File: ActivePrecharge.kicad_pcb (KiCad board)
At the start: 2 copper layers, 71 x 55 mm, 34 parts, among them Con1 LED, J1 Conn_01x03, J2 Conn_01x02, J3 Conn_01x02, Q1 IRLML0030, U1 NCP785AH50T1G, U2 NCP785AH50T1G, U3 TLV9301xDCK, U4 TCMT1106

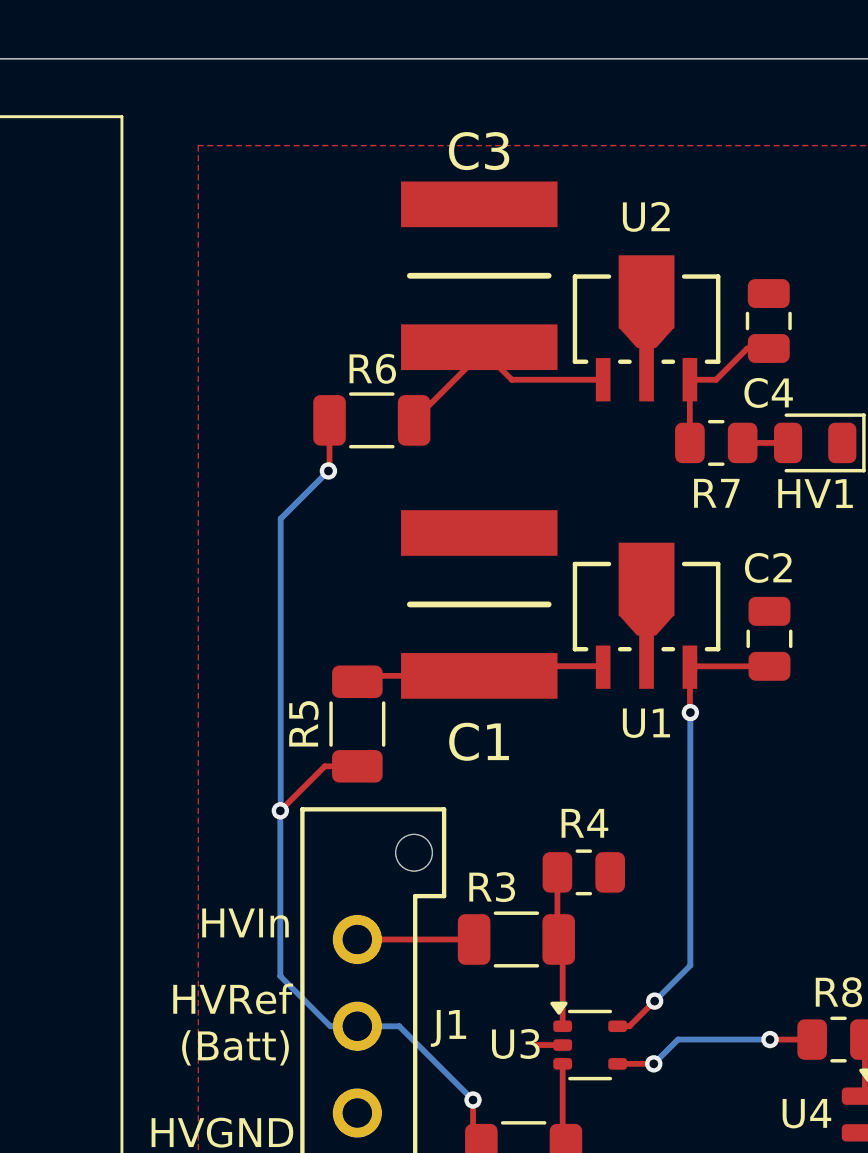
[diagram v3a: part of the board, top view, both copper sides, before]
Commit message: revert LDO HV resistor position
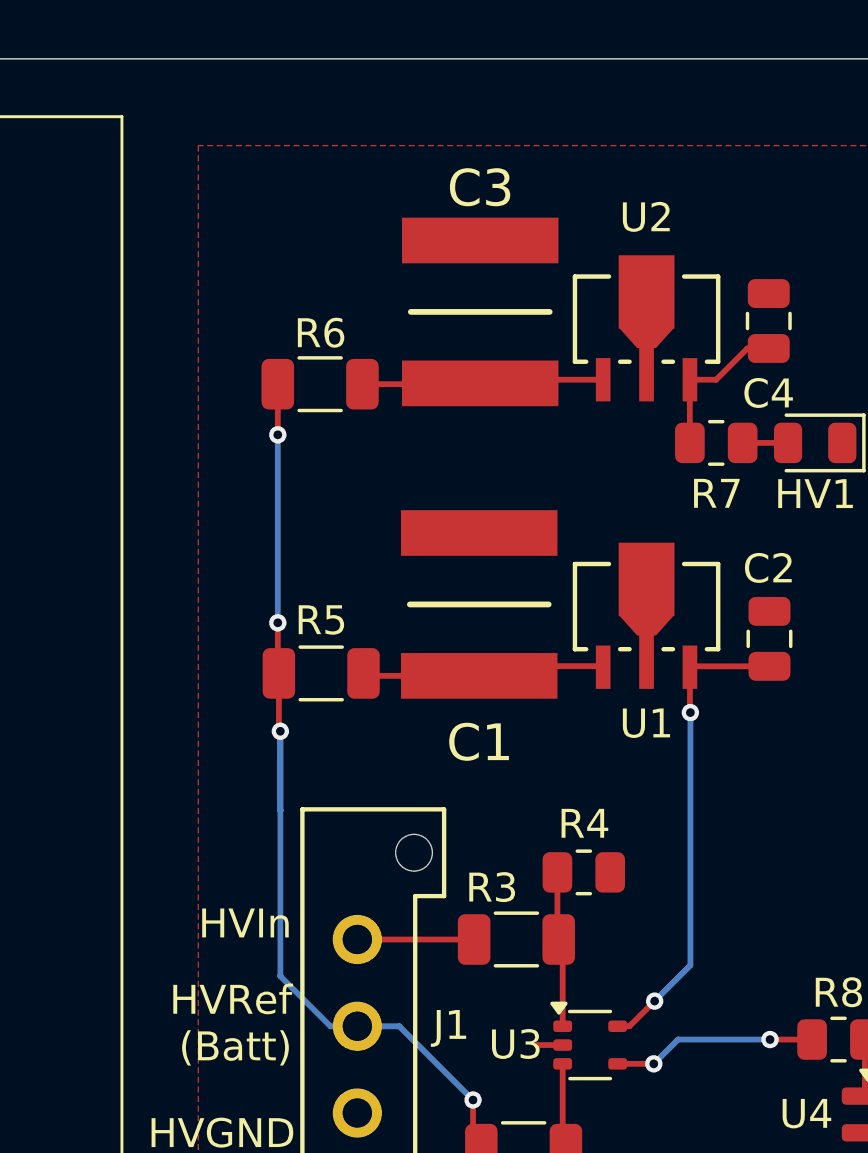
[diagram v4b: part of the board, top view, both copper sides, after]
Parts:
- moved R6 2.18 mm to (105.2, 79.2)
- moved R5 2.15 mm to (105.2, 89.2), turned to 0 degrees
- moved C3 1.25 mm to (110.8, 76.8)
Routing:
- net HVRef: track 33.5 -> 31.8 mm, vias 3 -> 4
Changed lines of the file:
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@@
 	(footprint "Active-PrechargeLib:CAPC5750X220N"
 		(layer "F.Cu")
-		(at 110.7155 75.5 90)
+		(at 110.75 76.75 90)
 		(descr "2220-1")
 		(tags "Capacitor")
@@
 	(footprint "Resistor_SMD:R_1206_3216Metric"
 		(layer "F.Cu")
-		(at 106.5 91 90)
+		(at 105.25 89.25)
 		(descr "Resistor SMD 1206 (3216 Metric), square (rectangular) end terminal, IPC_7351 nominal, (Body size source: IPC-SM-782 page 72, https://www.pcb-3d.com/wordpress/wp-content/uploads/ipc-sm-782a_amendment_1_and_2.pdf), generated with kicad-footprint-generator")
 		(tags "resistor")
 		(property "Reference" "R5"
-			(at 0 -1.82 90)
+			(at 0 -1.82 360)
 			(layer "F.SilkS")
 			(effects
@@
 		)
 		(property "Value" "10k"
-			(at 0 1.82 90)
+			(at 0 1.82 360)
 			(layer "F.Fab")
 			(effects
@@
 		)
 		(property "Footprint" "Resistor_SMD:R_1206_3216Metric"
-			(at 0 0 90)
+			(at 0 0 0)
 			(unlocked yes)
 			(layer "F.Fab")
@@
 		)
 		(property "Datasheet" ""
-			(at 0 0 90)
+			(at 0 0 0)
 			(unlocked yes)
 			(layer "F.Fab")
@@
 		)
 		(property "Description" "Resistor, US symbol"
-			(at 0 0 90)
+			(at 0 0 0)
 			(unlocked yes)
 			(layer "F.Fab")
@@
 		)
 		(fp_line
-			(start 2.28 -1.12)
-			(end 2.28 1.12)
+			(start -2.28 -1.12)
+			(end 2.28 -1.12)
 			(stroke
 				(width 0.05)
@@
 		)
 		(fp_line
-			(start -2.28 -1.12)
-			(end 2.28 -1.12)
+			(start -2.28 1.12)
+			(end -2.28 -1.12)
 			(stroke
 				(width 0.05)
@@
 		)
 		(fp_line
-			(start 2.28 1.12)
-			(end -2.28 1.12)
+			(start 2.28 -1.12)
+			(end 2.28 1.12)
 			(stroke
 				(width 0.05)
@@
 		)
 		(fp_line
-			(start -2.28 1.12)
-			(end -2.28 -1.12)
+			(start 2.28 1.12)
+			(end -2.28 1.12)
 			(stroke
 				(width 0.05)
@@
 		)
 		(fp_line
-			(start 1.6 -0.8)
-			(end 1.6 0.8)
+			(start -1.6 -0.8)
+			(end 1.6 -0.8)
 			(stroke
 				(width 0.1)
@@
 		)
 		(fp_line
-			(start -1.6 -0.8)
-			(end 1.6 -0.8)
+			(start -1.6 0.8)
+			(end -1.6 -0.8)
 			(stroke
 				(width 0.1)
@@
 		)
 		(fp_line
-			(start 1.6 0.8)
-			(end -1.6 0.8)
+			(start 1.6 -0.8)
+			(end 1.6 0.8)
 			(stroke
 				(width 0.1)
@@
 		)
 		(fp_line
-			(start -1.6 0.8)
-			(end -1.6 -0.8)
+			(start 1.6 0.8)
+			(end -1.6 0.8)
 			(stroke
 				(width 0.1)
@@
 		)
 		(fp_text user "${REFERENCE}"
-			(at 0 0 90)
+			(at 0 0 360)
 			(layer "F.Fab")
 			(effects
@@
 		)
 		(pad "1" smd roundrect
-			(at -1.4625 0 90)
+			(at -1.4625 0)
 			(size 1.125 1.75)
 			(layers "F.Cu" "F.Paste" "F.Mask")
@@
 		)
 		(pad "2" smd roundrect
-			(at 1.4625 0 90)
+			(at 1.4625 0)
 			(size 1.125 1.75)
 			(layers "F.Cu" "F.Paste" "F.Mask")
@@
 	(footprint "Resistor_SMD:R_1206_3216Metric"
 		(layer "F.Cu")
-		(at 107 80.5 180)
+		(at 105.2125 79.25 180)
 		(descr "Resistor SMD 1206 (3216 Metric), square (rectangular) end terminal, IPC_7351 nominal, (Body size source: IPC-SM-782 page 72, https://www.pcb-3d.com/wordpress/wp-content/uploads/ipc-sm-782a_amendment_1_and_2.pdf), generated with kicad-footprint-generator")
 		(tags "resistor")
@@
 	)
 	(gr_line
+		(start 103.75 81)
+		(end 103.75 79.25)
+		(stroke
+			(width 0.2)
+			(type default)
+		)
+		(layer "F.Cu")
+		(net 7)
+	)
+	(gr_line
 		(start 98.36 120.75)
 		(end 82 120.75)
@@
 	)
 	(segment
-		(start 105.375 92.4625)
-		(end 106.5 92.4625)
+		(start 103.7875 91.2)
+		(end 103.7875 89.25)
 		(width 0.2)
 		(layer "F.Cu")
@@
 	)
 	(segment
-		(start 105.5375 80.5)
-		(end 105.5375 82.2125)
+		(start 103.75 87.5)
+		(end 103.75 89.2125)
 		(width 0.2)
 		(layer "F.Cu")
@@
 	)
 	(segment
-		(start 105.5375 82.2125)
-		(end 105.5 82.25)
+		(start 103.8375 91.25)
+		(end 103.7875 91.2)
 		(width 0.2)
 		(layer "F.Cu")
@@
 	)
 	(segment
-		(start 103.8375 94)
-		(end 105.375 92.4625)
+		(start 103.75 89.2125)
+		(end 103.7875 89.25)
 		(width 0.2)
 		(layer "F.Cu")
@@
 	)
 	(via
-		(at 105.5 82.25)
+		(at 103.75 81)
 		(size 0.6)
 		(drill 0.3)
@@
 	)
 	(via
-		(at 103.8375 94)
+		(at 103.75 87.5)
+		(size 0.6)
+		(drill 0.3)
+		(layers "F.Cu" "B.Cu")
+		(net 7)
+	)
+	(via
+		(at 103.8375 91.25)
 		(size 0.6)
 		(drill 0.3)
@@
 	)
 	(segment
-		(start 103.8375 94)
+		(start 103.75 81)
+		(end 103.75 87.5)
+		(width 0.2)
+		(layer "B.Cu")
+		(net 7)
+	)
+	(segment
+		(start 103.8375 91.25)
 		(end 103.8375 99.7175)
 		(width 0.2)
@@
 	)
 	(segment
-		(start 103.85 93.9875)
-		(end 103.85 83.9)
+		(start 103.8375 99.7175)
+		(end 105.57 101.45)
 		(width 0.2)
 		(layer "B.Cu")
@@
 	)
 	(segment
-		(start 103.8375 94)
+		(start 103.8375 93.975)
 		(end 103.85 93.9875)
 		(width 0.2)
@@
 	)
 	(segment
-		(start 103.8375 99.7175)
-		(end 105.57 101.45)
+		(start 103.8375 91.25)
+		(end 103.8375 93.975)
 		(width 0.2)
 		(layer "B.Cu")
@@
 	)
 	(segment
-		(start 103.85 83.9)
-		(end 105.5 82.25)
-		(width 0.2)
-		(layer "B.Cu")
-		(net 7)
-	)
-	(segment
 		(start 110.5375 98.45)
 		(end 106.5 98.45)
@@
 	)
 	(segment
-		(start 115 79.0955)
-		(end 111.841 79.0955)
+		(start 110.72 79.25)
+		(end 110.75 79.22)
 		(width 0.2)
 		(layer "F.Cu")
@@
 	)
 	(segment
-		(start 111.841 79.0955)
-		(end 110.7155 77.97)
+		(start 115 79.0955)
+		(end 110.8745 79.0955)
 		(width 0.2)
 		(layer "F.Cu")
@@
 	)
 	(segment
-		(start 108.4625 80.5)
-		(end 110.7155 78.247)
+		(start 110.8745 79.0955)
+		(end 110.75 79.22)
 		(width 0.2)
 		(layer "F.Cu")
@@
 	)
 	(segment
-		(start 110.7155 78.247)
-		(end 110.7155 77.97)
+		(start 106.675 79.25)
+		(end 110.72 79.25)
 		(width 0.2)
 		(layer "F.Cu")

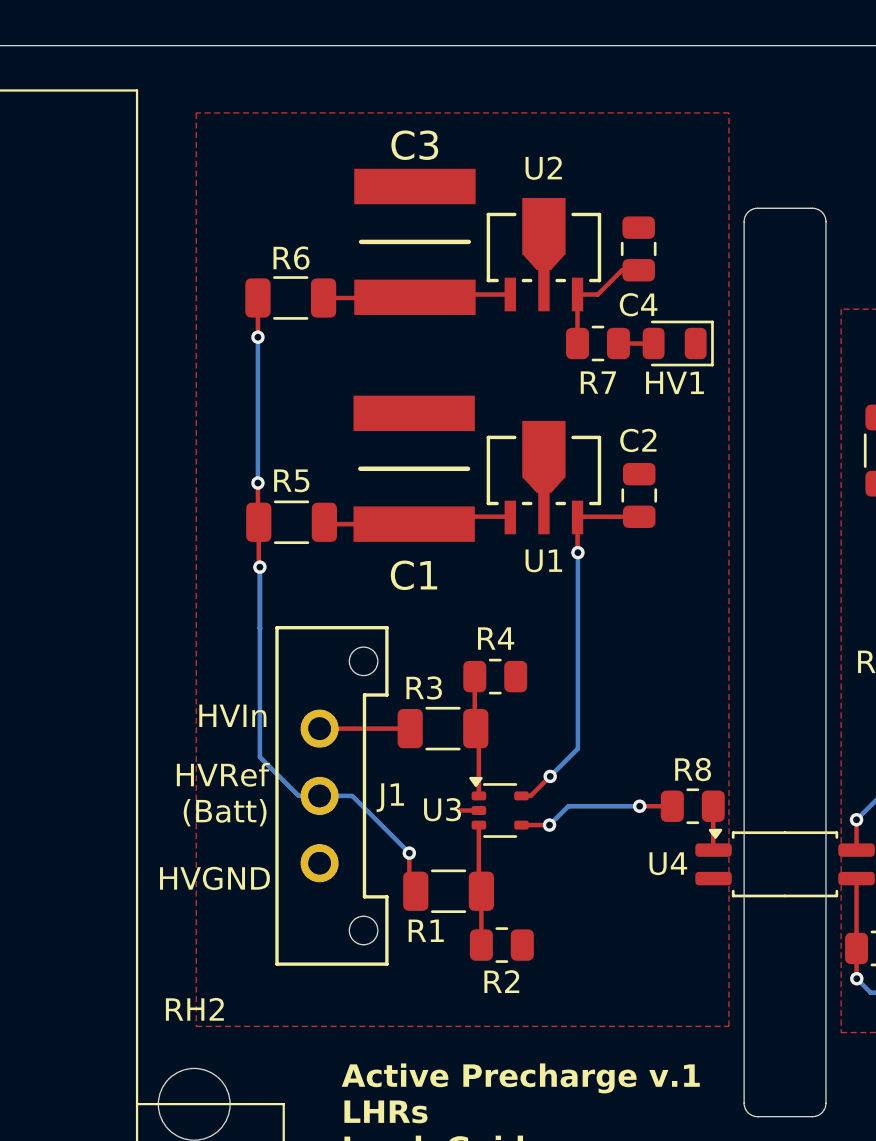
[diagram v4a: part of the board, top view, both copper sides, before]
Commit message: adjusted HVGND position to be more centralized, added backplane traces and vias to route HVGND up to somewhat isolated top region, routed R1, R3 top plane traces on the back
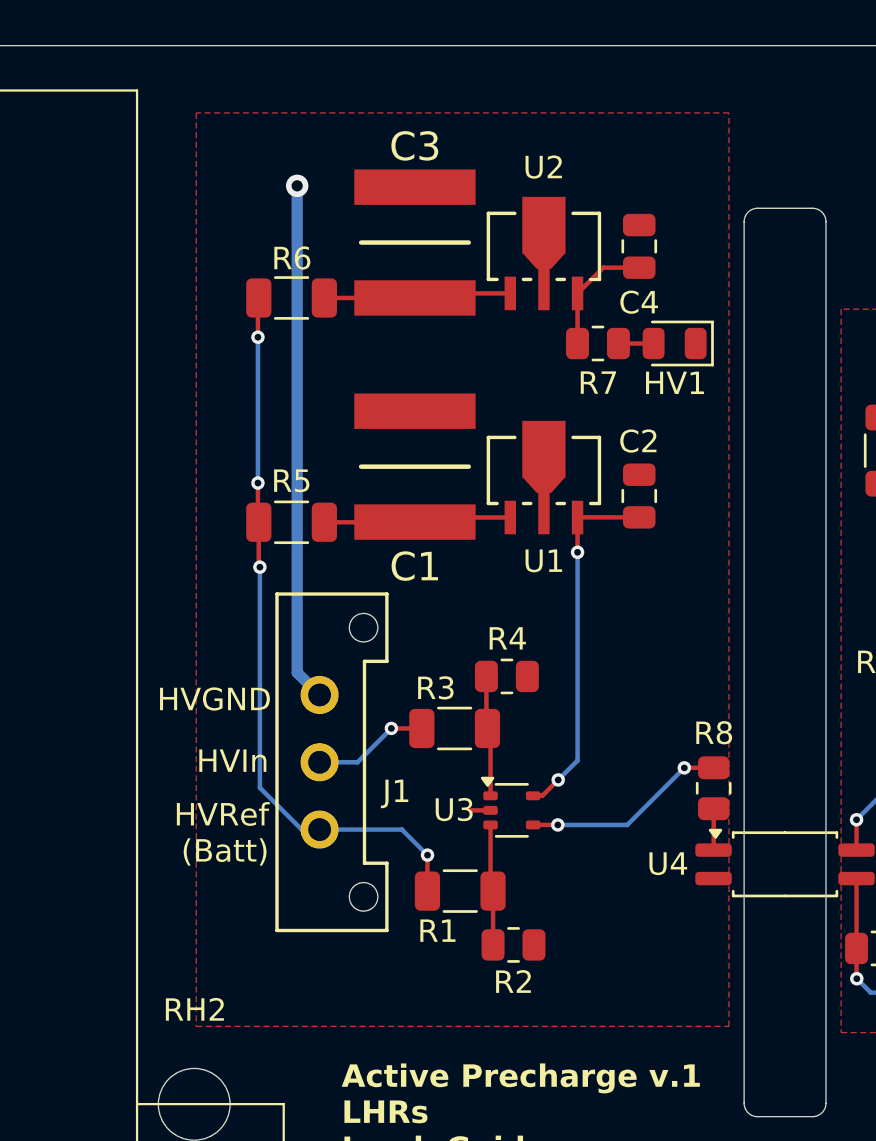
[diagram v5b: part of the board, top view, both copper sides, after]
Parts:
- moved J1 1.50 mm to (106.5, 97.0)
- moved R8 1.23 mm to (124.1, 101.1), turned to -90 degrees
- moved R1 0.52 mm to (112.8, 105.7)
- moved R3 0.52 mm to (112.5, 98.4)
- moved R2 0.52 mm to (115.1, 108.1)
- moved R4 0.52 mm to (114.8, 96.1)
- moved U3 0.52 mm to (115.1, 102.1)
- moved C4 0.12 mm to (120.8, 77.0)
- moved C1 0.10 mm to (110.8, 86.8)
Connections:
- J1 pad 1: /HVIn -> HVGND
- J1 pad 2: HVRef -> /HVIn
- J1 pad 3: HVGND -> HVRef
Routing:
- net HVGND: track 0.90 -> 24.0 mm, vias 0 -> 1
- net /SignalHV: track 7.07 -> 9.11 mm
- net HVRef: track 31.8 -> 30.4 mm
- net /HVIn: track 4.04 -> 5.18 mm, vias 0 -> 1
